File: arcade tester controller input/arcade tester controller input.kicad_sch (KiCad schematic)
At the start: 25 parts, among them J1 FTDI, J2 ICSP, J3 DE9M 1, J4 DE9M 2, J5 Conn_01x08, J6 Conn_01x08, J7 Conn_01x08, J8 Conn_01x08, J9 Conn_01x02, U1 ATmega328P-P, U2 MCP23018, U3 MCP23018, Y1 16M

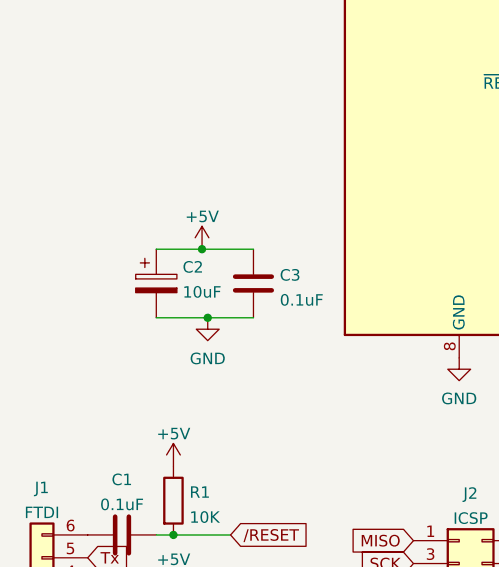
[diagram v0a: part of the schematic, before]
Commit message: made pcb for pci bracket board
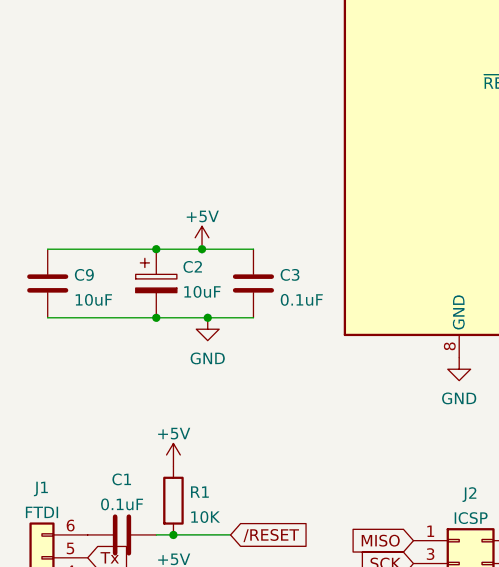
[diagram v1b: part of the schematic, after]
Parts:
- added C9: 10uF, Capacitor_SMD:C_0603_1608Metric, symbol Device:C
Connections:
- net +5V: now also C9.1
- net GND: now also C9.2
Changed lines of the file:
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@@
   (junction (at 38.1 93.98) (diameter 0) (color 0 0 0 0)
+  )
+  (junction (at 33.02 101.6) (diameter 0) (color 0 0 0 0)
+  )
+  (junction (at 33.02 93.98) (diameter 0) (color 0 0 0 0)
   )
   (junction (at 100.33 58.42) (diameter 0) (color 0 0 0 0)
@@
     (stroke (width 0) (type default) (color 0 0 0 0))
   )
+  (wire (pts (xy 33.02 101.6) (xy 38.735 101.6))
+    (stroke (width 0) (type default) (color 0 0 0 0))
+  )
+  (wire (pts (xy 33.02 93.98) (xy 38.1 93.98))
+    (stroke (width 0) (type default) (color 0 0 0 0))
+  )
   (wire (pts (xy 88.9 42.545) (xy 88.9 45.085))
     (stroke (width 0) (type default) (color 0 0 0 0))
@@
     (stroke (width 0) (type default) (color 0 0 0 0))
   )
-  (wire (pts (xy 33.02 101.6) (xy 38.735 101.6))
+  (wire (pts (xy 20.955 101.6) (xy 33.02 101.6))
     (stroke (width 0) (type default) (color 0 0 0 0))
   )
@@
     (stroke (width 0) (type default) (color 0 0 0 0))
   )
-  (wire (pts (xy 33.02 93.98) (xy 38.1 93.98))
+  (wire (pts (xy 20.955 93.98) (xy 33.02 93.98))
     (stroke (width 0) (type default) (color 0 0 0 0))
   )
@@
     )
     (property "Datasheet" "~" (id 3) (at 45.085 41.275 0)
+      (effects (font (size 1.27 1.27)) hide)
+    )
+    (pin "1")
+    (pin "2")
+  )
+  (symbol (lib_id "Device:C") (at 20.955 97.79 0) (unit 1)
+    (in_bom yes) (on_board yes) (fields_autoplaced)
+    (property "Reference" "C9" (id 0) (at 23.876 96.8815 0)
+      (effects (font (size 1.27 1.27)) (justify left))
+    )
+    (property "Value" "10uF" (id 1) (at 23.876 99.6566 0)
+      (effects (font (size 1.27 1.27)) (justify left))
+    )
+    (property "Footprint" "Capacitor_SMD:C_0603_1608Metric" (id 2) (at 21.9202 101.6 0)
+      (effects (font (size 1.27 1.27)) hide)
+    )
+    (property "Datasheet" "~" (id 3) (at 20.955 97.79 0)
       (effects (font (size 1.27 1.27)) hide)
     )
@@
       (reference "C8") (unit 1) (value "0.1uF") (footprint "Capacitor_SMD:C_0603_1608Metric")
     )
+    (path "/2b77f9da-f17d-4e9a-800a-449426ecabc6"
+      (reference "C9") (unit 1) (value "10uF") (footprint "Capacitor_SMD:C_0603_1608Metric")
+    )
     (path "/2cf6b0ba-51fa-4cb2-808f-73ea4d1ab172"

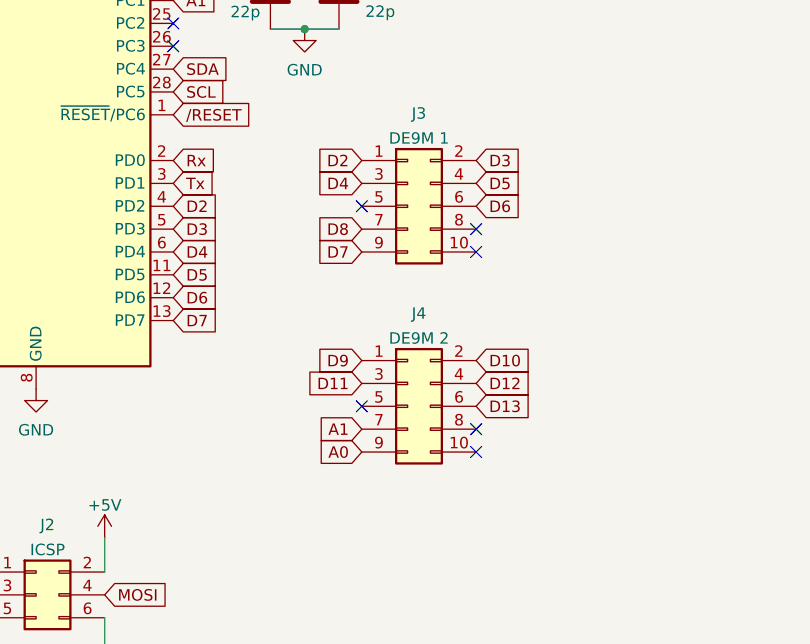
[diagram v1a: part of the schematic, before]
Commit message: added 5v and gnd to controller ports
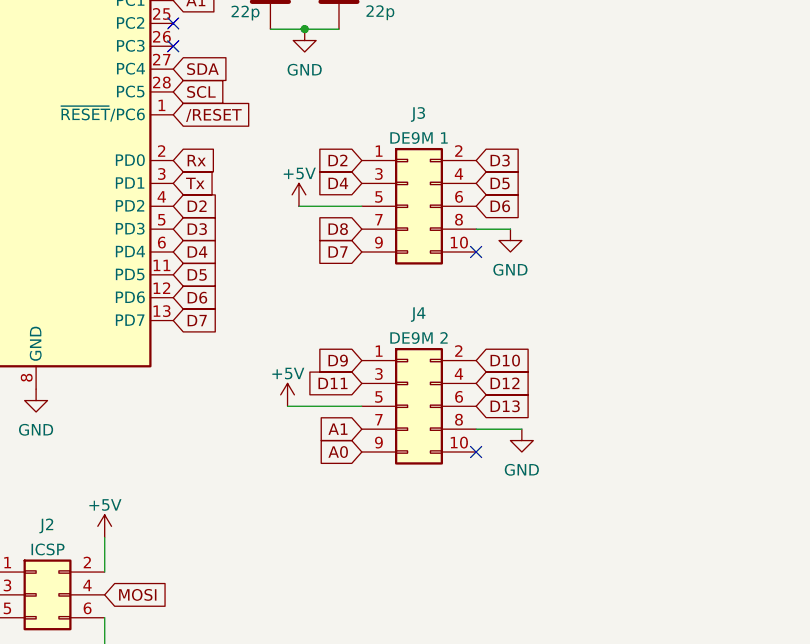
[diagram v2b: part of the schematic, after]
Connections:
- net +5V: now also J3.5 (Pin_5), J4.5 (Pin_5)
- net GND: now also J3.8 (Pin_8), J4.8 (Pin_8)
- no-connect marks 12 -> 8
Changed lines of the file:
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@@
   (junction (at 25.4 138.43) (diameter 0) (color 0 0 0 0)
   )
-  (no_connect (at 115.57 88.265))
-  (no_connect (at 102.87 85.725))
-  (no_connect (at 115.57 110.49))
-  (no_connect (at 102.87 107.95))
   (no_connect (at 189.23 121.285))
   (no_connect (at 189.23 123.825))
@@
     (stroke (width 0) (type default) (color 0 0 0 0))
   )
+  (wire (pts (xy 115.57 88.265) (xy 119.38 88.265))
+    (stroke (width 0) (type default) (color 0 0 0 0))
+  )
+  (wire (pts (xy 94.615 107.95) (xy 102.87 107.95))
+    (stroke (width 0) (type default) (color 0 0 0 0))
+  )
   (wire (pts (xy 185.42 60.96) (xy 188.595 60.96))
     (stroke (width 0) (type default) (color 0 0 0 0))
@@
     (stroke (width 0) (type default) (color 0 0 0 0))
   )
+  (wire (pts (xy 95.885 85.725) (xy 102.87 85.725))
+    (stroke (width 0) (type default) (color 0 0 0 0))
+  )
   (wire (pts (xy 95.885 47.625) (xy 81.915 47.625))
     (stroke (width 0) (type default) (color 0 0 0 0))
   )
   (wire (pts (xy 34.925 125.73) (xy 33.02 125.73))
+    (stroke (width 0) (type default) (color 0 0 0 0))
+  )
+  (wire (pts (xy 115.57 110.49) (xy 120.65 110.49))
     (stroke (width 0) (type default) (color 0 0 0 0))
   )
@@
     )
     (property "Datasheet" "" (id 3) (at 186.055 128.905 0)
+      (effects (font (size 1.27 1.27)) hide)
+    )
+    (pin "1")
+  )
+  (symbol (lib_id "power:+5V") (at 95.885 85.725 0) (unit 1)
+    (in_bom yes) (on_board yes) (fields_autoplaced)
+    (property "Reference" "#PWR?" (id 0) (at 95.885 89.535 0)
+      (effects (font (size 1.27 1.27)) hide)
+    )
+    (property "Value" "+5V" (id 1) (at 95.885 82.1205 0))
+    (property "Footprint" "" (id 2) (at 95.885 85.725 0)
+      (effects (font (size 1.27 1.27)) hide)
+    )
+    (property "Datasheet" "" (id 3) (at 95.885 85.725 0)
       (effects (font (size 1.27 1.27)) hide)
     )
@@
     (pin "1")
   )
+  (symbol (lib_id "power:GND") (at 119.38 88.265 0) (unit 1)
+    (in_bom yes) (on_board yes) (fields_autoplaced)
+    (property "Reference" "#PWR?" (id 0) (at 119.38 94.615 0)
+      (effects (font (size 1.27 1.27)) hide)
+    )
+    (property "Value" "GND" (id 1) (at 119.38 92.8275 0))
+    (property "Footprint" "" (id 2) (at 119.38 88.265 0)
+      (effects (font (size 1.27 1.27)) hide)
+    )
+    (property "Datasheet" "" (id 3) (at 119.38 88.265 0)
+      (effects (font (size 1.27 1.27)) hide)
+    )
+    (pin "1")
+  )
   (symbol (lib_id "Device:R") (at 182.88 82.55 0) (unit 1)
     (in_bom yes) (on_board yes) (fields_autoplaced)
@@
     )
     (property "Datasheet" "" (id 3) (at 38.735 101.6 0)
+      (effects (font (size 1.27 1.27)) hide)
+    )
+    (pin "1")
+  )
+  (symbol (lib_id "power:+5V") (at 94.615 107.95 0) (unit 1)
+    (in_bom yes) (on_board yes) (fields_autoplaced)
+    (property "Reference" "#PWR?" (id 0) (at 94.615 111.76 0)
+      (effects (font (size 1.27 1.27)) hide)
+    )
+    (property "Value" "+5V" (id 1) (at 94.615 104.3455 0))
+    (property "Footprint" "" (id 2) (at 94.615 107.95 0)
+      (effects (font (size 1.27 1.27)) hide)
+    )
+    (property "Datasheet" "" (id 3) (at 94.615 107.95 0)
       (effects (font (size 1.27 1.27)) hide)
     )
@@
     (pin "1")
   )
+  (symbol (lib_id "power:GND") (at 120.65 110.49 0) (unit 1)
+    (in_bom yes) (on_board yes) (fields_autoplaced)
+    (property "Reference" "#PWR?" (id 0) (at 120.65 116.84 0)
+      (effects (font (size 1.27 1.27)) hide)
+    )
+    (property "Value" "GND" (id 1) (at 120.65 115.0525 0))
+    (property "Footprint" "" (id 2) (at 120.65 110.49 0)
+      (effects (font (size 1.27 1.27)) hide)
+    )
+    (property "Datasheet" "" (id 3) (at 120.65 110.49 0)
+      (effects (font (size 1.27 1.27)) hide)
+    )
+    (pin "1")
+  )
   (symbol (lib_id "Device:C") (at 170.815 147.32 0) (unit 1)
     (in_bom yes) (on_board yes) (fields_autoplaced)
@@
       (reference "#PWR0102") (unit 1) (value "GND") (footprint "")
     )
+    (path "/05be4c58-5113-4a3e-bdb4-5fad760bd078"
+      (reference "#PWR?") (unit 1) (value "+5V") (footprint "")
+    )
+    (path "/64f47ae4-bf36-4413-ae6b-9a7d3a1e59da"
+      (reference "#PWR?") (unit 1) (value "GND") (footprint "")
+    )
+    (path "/812d64fc-5b6c-4013-ace7-40b1d6d957a7"
+      (reference "#PWR?") (unit 1) (value "+5V") (footprint "")
+    )
+    (path "/db5eee57-71a9-41d2-84ae-3a208d9127dc"
+      (reference "#PWR?") (unit 1) (value "GND") (footprint "")
+    )
     (path "/6aaa0eb7-bc0c-4535-a7cc-9182343b6675"
